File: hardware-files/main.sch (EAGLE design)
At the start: 27 parts, among them IC3 E73_2G4M04S, J4 SCREWTERMINAL_3X, Q1 BUZ11, Q2 BUZ11, Q3 BUZ11, Q4 BUZ11

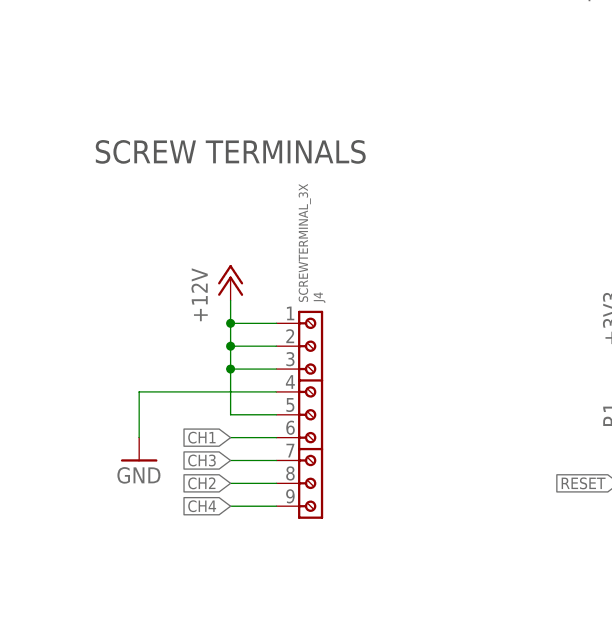
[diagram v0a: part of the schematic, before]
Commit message: added dc barrel jack
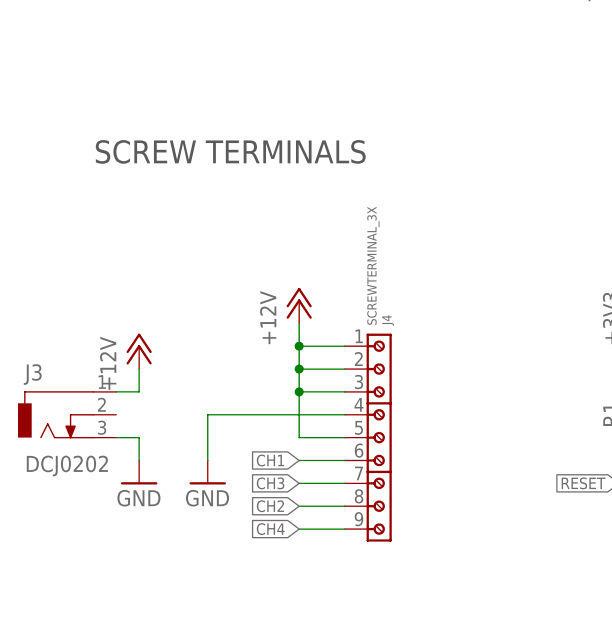
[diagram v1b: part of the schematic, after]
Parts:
- added J3: DCJ0202, con-jack:DCJ0202
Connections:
- net +12V: now also J3.1
- net GND: now also J3.3
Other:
- moved on the sheet: J4
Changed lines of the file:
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@@
 <part name="J4" library="Eigene Bauteile" library_urn="urn:adsk.eagle:library:2511163" deviceset="SCREWTERMINAL_3X" device="" override_package3d_urn="urn:adsk.eagle:package:24172144/2" override_package_urn="urn:adsk.eagle:footprint:24172145/1"/>
 <part name="P+1" library="C_Supply" deviceset="+12V" device=""/>
+<part name="J3" library="con-jack" library_urn="urn:adsk.eagle:library:154" deviceset="DCJ0202" device="" package3d_urn="urn:adsk.eagle:package:7491/1" override_package3d_urn="urn:adsk.eagle:package:24228003/2" override_package_urn="urn:adsk.eagle:footprint:7486/1"/>
+<part name="P+3" library="C_Supply" deviceset="+12V" device=""/>
+<part name="GND12" library="supply1" library_urn="urn:adsk.eagle:library:371" deviceset="GND" device=""/>
 </parts>
 <sheets>
@@
 <attribute name="VALUE" x="58.42" y="96.52" size="1.778" layer="96"/>
 </instance>
-<instance part="GND3" gate="1" x="30.48" y="38.1" smashed="yes">
-<attribute name="VALUE" x="27.94" y="35.56" size="1.778" layer="96"/>
+<instance part="GND3" gate="1" x="38.1" y="35.56" smashed="yes">
+<attribute name="VALUE" x="35.56" y="33.02" size="1.778" layer="96"/>
 </instance>
 <instance part="R2" gate="G$1" x="30.48" y="137.16" smashed="yes">
@@
 <attribute name="VALUE" x="238.76" y="76.2" size="1.778" layer="96" rot="MR0"/>
 </instance>
-<instance part="J4" gate="B" x="50.8" y="43.18" smashed="yes" rot="R270">
-<attribute name="NAME" x="49.878" y="55.68" size="1.016" layer="95" rot="R270" align="bottom-right"/>
-<attribute name="VALUE" x="48.22" y="55.63" size="1.016" layer="96" rot="R270" align="bottom-right"/>
-</instance>
-<instance part="P+1" gate="1" x="40.64" y="58.42" smashed="yes">
-<attribute name="VALUE" x="38.1" y="53.34" size="1.778" layer="96" rot="R90"/>
+<instance part="J4" gate="B" x="58.42" y="40.64" smashed="yes" rot="R270">
+<attribute name="NAME" x="57.498" y="53.14" size="1.016" layer="95" rot="R270" align="bottom-right"/>
+<attribute name="VALUE" x="55.84" y="53.09" size="1.016" layer="96" rot="R270" align="bottom-right"/>
+</instance>
+<instance part="P+1" gate="1" x="48.26" y="55.88" smashed="yes">
+<attribute name="VALUE" x="45.72" y="50.8" size="1.778" layer="96" rot="R90"/>
+</instance>
+<instance part="J3" gate="G$1" x="20.32" y="43.18" smashed="yes">
+<attribute name="NAME" x="17.78" y="46.99" size="1.778" layer="95"/>
+<attribute name="VALUE" x="17.78" y="36.83" size="1.778" layer="96"/>
+</instance>
+<instance part="P+3" gate="1" x="30.48" y="50.8" smashed="yes">
+<attribute name="VALUE" x="27.94" y="45.72" size="1.778" layer="96" rot="R90"/>
+</instance>
+<instance part="GND12" gate="1" x="30.48" y="35.56" smashed="yes">
+<attribute name="VALUE" x="27.94" y="33.02" size="1.778" layer="96"/>
 </instance>
 </instances>
@@
 <pinref part="GND3" gate="1" pin="GND"/>
 <pinref part="J4" gate="B" pin="4"/>
-<wire x1="45.72" y1="45.72" x2="30.48" y2="45.72" width="0.1524" layer="91"/>
-<wire x1="30.48" y1="45.72" x2="30.48" y2="40.64" width="0.1524" layer="91"/>
+<wire x1="53.34" y1="43.18" x2="38.1" y2="43.18" width="0.1524" layer="91"/>
+<wire x1="38.1" y1="43.18" x2="38.1" y2="38.1" width="0.1524" layer="91"/>
 </segment>
 <segment>
@@
 <wire x1="243.84" y1="68.58" x2="246.38" y2="68.58" width="0.1524" layer="91"/>
 </segment>
+<segment>
+<pinref part="J3" gate="G$1" pin="3"/>
+<pinref part="GND12" gate="1" pin="GND"/>
+<wire x1="27.94" y1="40.64" x2="30.48" y2="40.64" width="0.1524" layer="91"/>
+<wire x1="30.48" y1="40.64" x2="30.48" y2="38.1" width="0.1524" layer="91"/>
+</segment>
 </net>
 <net name="TX" class="0">
@@
 <net name="CH4" class="0">
 <segment>
-<wire x1="45.72" y1="33.02" x2="40.64" y2="33.02" width="0.1524" layer="91"/>
-<label x="40.64" y="33.02" size="1.27" layer="95" rot="R180" xref="yes"/>
+<wire x1="53.34" y1="30.48" x2="48.26" y2="30.48" width="0.1524" layer="91"/>
+<label x="48.26" y="30.48" size="1.27" layer="95" rot="R180" xref="yes"/>
 <pinref part="J4" gate="B" pin="9"/>
 </segment>
@@
 </segment>
 <segment>
-<wire x1="45.72" y1="38.1" x2="40.64" y2="38.1" width="0.1524" layer="91"/>
-<label x="40.64" y="38.1" size="1.27" layer="95" rot="R180" xref="yes"/>
+<wire x1="53.34" y1="35.56" x2="48.26" y2="35.56" width="0.1524" layer="91"/>
+<label x="48.26" y="35.56" size="1.27" layer="95" rot="R180" xref="yes"/>
 <pinref part="J4" gate="B" pin="7"/>
 </segment>
@@
 </segment>
 <segment>
-<wire x1="45.72" y1="35.56" x2="40.64" y2="35.56" width="0.1524" layer="91"/>
-<label x="40.64" y="35.56" size="1.27" layer="95" rot="R180" xref="yes"/>
+<wire x1="53.34" y1="33.02" x2="48.26" y2="33.02" width="0.1524" layer="91"/>
+<label x="48.26" y="33.02" size="1.27" layer="95" rot="R180" xref="yes"/>
 <pinref part="J4" gate="B" pin="8"/>
 </segment>
@@
 <net name="CH1" class="0">
 <segment>
-<wire x1="45.72" y1="40.64" x2="40.64" y2="40.64" width="0.1524" layer="91"/>
-<label x="40.64" y="40.64" size="1.27" layer="95" rot="R180" xref="yes"/>
+<wire x1="53.34" y1="38.1" x2="48.26" y2="38.1" width="0.1524" layer="91"/>
+<label x="48.26" y="38.1" size="1.27" layer="95" rot="R180" xref="yes"/>
 <pinref part="J4" gate="B" pin="6"/>
 </segment>
@@
 <pinref part="P+1" gate="1" pin="+12V"/>
 <pinref part="J4" gate="B" pin="3"/>
-<wire x1="40.64" y1="48.26" x2="40.64" y2="50.8" width="0.1524" layer="91"/>
-<wire x1="40.64" y1="50.8" x2="40.64" y2="53.34" width="0.1524" layer="91"/>
-<wire x1="40.64" y1="53.34" x2="40.64" y2="55.88" width="0.1524" layer="91"/>
-<wire x1="45.72" y1="48.26" x2="40.64" y2="48.26" width="0.1524" layer="91"/>
-<junction x="40.64" y="48.26"/>
+<wire x1="48.26" y1="45.72" x2="48.26" y2="48.26" width="0.1524" layer="91"/>
+<wire x1="48.26" y1="48.26" x2="48.26" y2="50.8" width="0.1524" layer="91"/>
+<wire x1="48.26" y1="50.8" x2="48.26" y2="53.34" width="0.1524" layer="91"/>
+<wire x1="53.34" y1="45.72" x2="48.26" y2="45.72" width="0.1524" layer="91"/>
+<junction x="48.26" y="45.72"/>
 <pinref part="J4" gate="B" pin="2"/>
-<wire x1="45.72" y1="50.8" x2="40.64" y2="50.8" width="0.1524" layer="91"/>
-<junction x="40.64" y="50.8"/>
+<wire x1="53.34" y1="48.26" x2="48.26" y2="48.26" width="0.1524" layer="91"/>
+<junction x="48.26" y="48.26"/>
 <pinref part="J4" gate="B" pin="1"/>
-<wire x1="45.72" y1="53.34" x2="40.64" y2="53.34" width="0.1524" layer="91"/>
-<junction x="40.64" y="53.34"/>
+<wire x1="53.34" y1="50.8" x2="48.26" y2="50.8" width="0.1524" layer="91"/>
+<junction x="48.26" y="50.8"/>
 <pinref part="J4" gate="B" pin="5"/>
-<wire x1="45.72" y1="43.18" x2="40.64" y2="43.18" width="0.1524" layer="91"/>
-<wire x1="40.64" y1="43.18" x2="40.64" y2="48.26" width="0.1524" layer="91"/>
-</segment>
-</net>
+<wire x1="53.34" y1="40.64" x2="48.26" y2="40.64" width="0.1524" layer="91"/>
+<wire x1="48.26" y1="40.64" x2="48.26" y2="45.72" width="0.1524" layer="91"/>
+</segment>
+<segment>
+<pinref part="J3" gate="G$1" pin="1"/>
+<pinref part="P+3" gate="1" pin="+12V"/>
+<wire x1="27.94" y1="45.72" x2="30.48" y2="45.72" width="0.1524" layer="91"/>
+<wire x1="30.48" y1="45.72" x2="30.48" y2="48.26" width="0.1524" layer="91"/>
+</segment>
+</net>
